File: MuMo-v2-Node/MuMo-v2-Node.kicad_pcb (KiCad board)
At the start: 2 copper layers, 52.1 x 50 mm, 76 parts, among them Q1 Si1308EDL, SW1 Boot0, SW2 Reset, U1 MCP73123, U2 LoRa-E5, U3 CP2102N, U4 eInk_Display_1.54"200x200px, U5 BME680, U6 TSL25911, U7 BR24G512FVT-5AE2

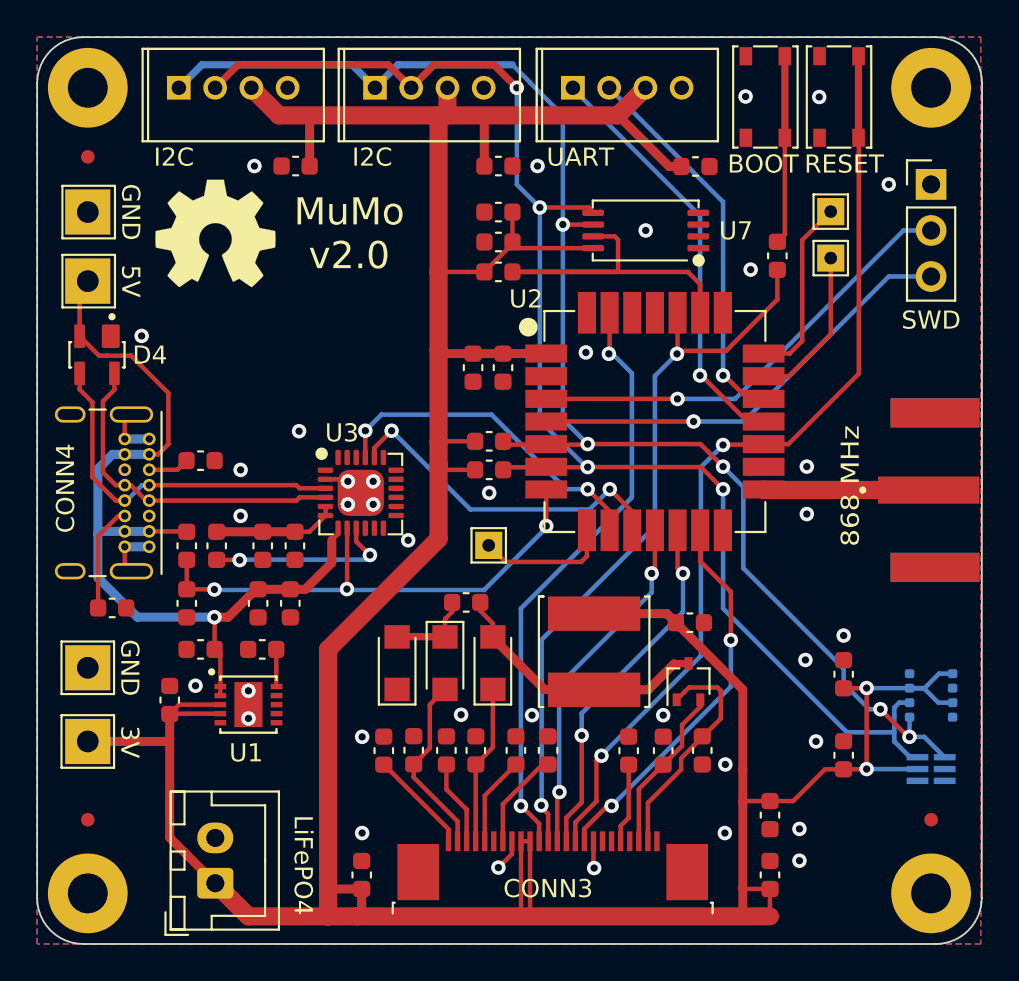
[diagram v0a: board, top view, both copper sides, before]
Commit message: fixed #1
Replaced GCT4085 connector with Molex 2171790001
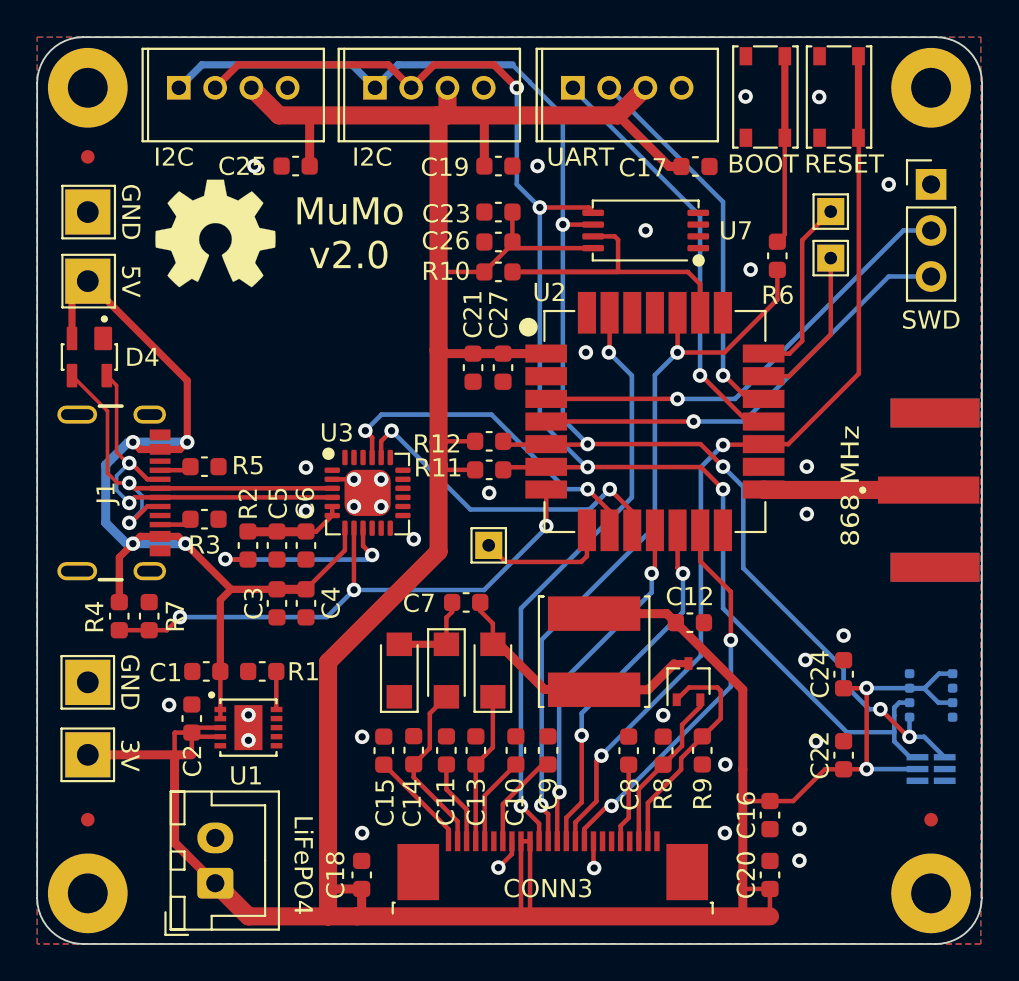
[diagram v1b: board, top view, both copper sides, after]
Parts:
- removed CONN4: USB-C, thisProjectLibrary:USB_C_Receptacle_GCT_USB4085
- added J1: USB4105-GF-A, thisProjectLibrary:Molex-2171790001, F.Cu at (144.8, 82.8)
- C1, C10, C11, C12, C13, C14, C15, C16, C17, C18, C19, C2, C20, C21, C22, C23, C24, C25, C26, C27, C3, C4, C5, C6, C7, C8, C9, R1, R10, R11, R12, R2, R3, R4, R5, R6, R7, R8, R9: footprint Capacitor_SMD:C_0603_1608Metric -> thisProjectLibrary:0603_1608Metric
- moved R5 9.31 mm to (152.0, 81.4), turned to 180 degrees
- moved R4 5.38 mm to (147.3, 89.6)
- moved R3 3.24 mm to (152.0, 84.3), turned to 180 degrees
- moved R7 2.19 mm to (148.9, 89.6), turned to 90 degrees
- moved R2 1.73 mm to (154.4, 85.7)
- moved C2 1.59 mm to (151.3, 95.3)
- moved U1 1.27 mm to (154.4, 95.8)
- moved C1 1.26 mm to (152.1, 92.7)
- moved R1 1.22 mm to (155.2, 92.7)
- moved C3 1.04 mm to (156.0, 88.9)
- moved C4 0.86 mm to (157.6, 88.9)
- moved TP4 0.80 mm to (145.5, 93.3)
- moved C5 0.79 mm to (156.0, 85.7)
- moved TP6 0.74 mm to (145.5, 97.3)
- moved C6 0.61 mm to (157.6, 85.7)
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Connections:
- net Net-(CONN4-PadA6) renamed D+
- net Net-(CONN4-PadA7) renamed D-
- R3 pad 1: Net-(CONN4-PadA5) -> GND
- R3 pad 2: GND -> Net-(J1-PadB5)
- R5 pad 1: Net-(CONN4-PadB5) -> GND
- R5 pad 2: GND -> Net-(J1-PadA5)
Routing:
- net +5V: track 49.3 -> 57.2 mm, vias 1 -> 4
- net Net-(CONN4-PadB5): track 5.89 -> 0.00 mm
- net GND: track 10.2 -> 5.51 mm, vias 37 -> 33
- net D+: track 19.8 -> 23.8 mm, vias 0 -> 2
- net VBUS: track 28.4 -> 31.4 mm
- net D-: track 18.7 -> 21.6 mm, vias 0 -> 2
- net Net-(CONN4-PadA5): track 2.27 -> 0.00 mm
- net Net-(J1-PadB5): track 0.00 -> 1.79 mm
- net Net-(J1-PadA5): track 0.00 -> 1.75 mm
- net 3V: track 6.88 -> 5.53 mm
- net RST: track 10.4 -> 11.2 mm
- net Net-(C7-Pad2): track 14.8 -> 15.5 mm

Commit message: Implemented improvements
#5 stitching vias
#4 USB differential pair
#6 components / values for epaper driver circuit
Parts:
- CONN2: value LiFePO4 Battery -> B2B-XH-A (LF)(SN)
- CONN4: renamed from J1; value USB4105-GF-A -> Molex-2171790001
- moved Q1 0.60 mm to (178.3, 93.7), turned to 180 degrees
- moved L1 0.58 mm to (172.9, 91.6)
- moved C12 0.51 mm to (178.8, 89.5)
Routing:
- net Net-(CONN3-Pad2): track 12.8 -> 9.04 mm
- net 3V: track 5.53 -> 7.09 mm
- net Net-(CONN3-Pad3): track 9.22 -> 10.4 mm
- net +3V3: track 228.7 -> 229.6 mm
- net Net-(C7-Pad2): track 15.5 -> 14.7 mm
- net GND: vias 33 -> 53
